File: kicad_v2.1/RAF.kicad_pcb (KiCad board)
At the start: 2 copper layers, 68.6 x 53.3 mm, 44 parts, among them J1 SERVO, J2 SERVO, J3 SOL, J4 SERVO, J5 PUMP, J6 WS2811-OUT, J7 I2C, P1 Power, P2 Analog, P3 Digital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

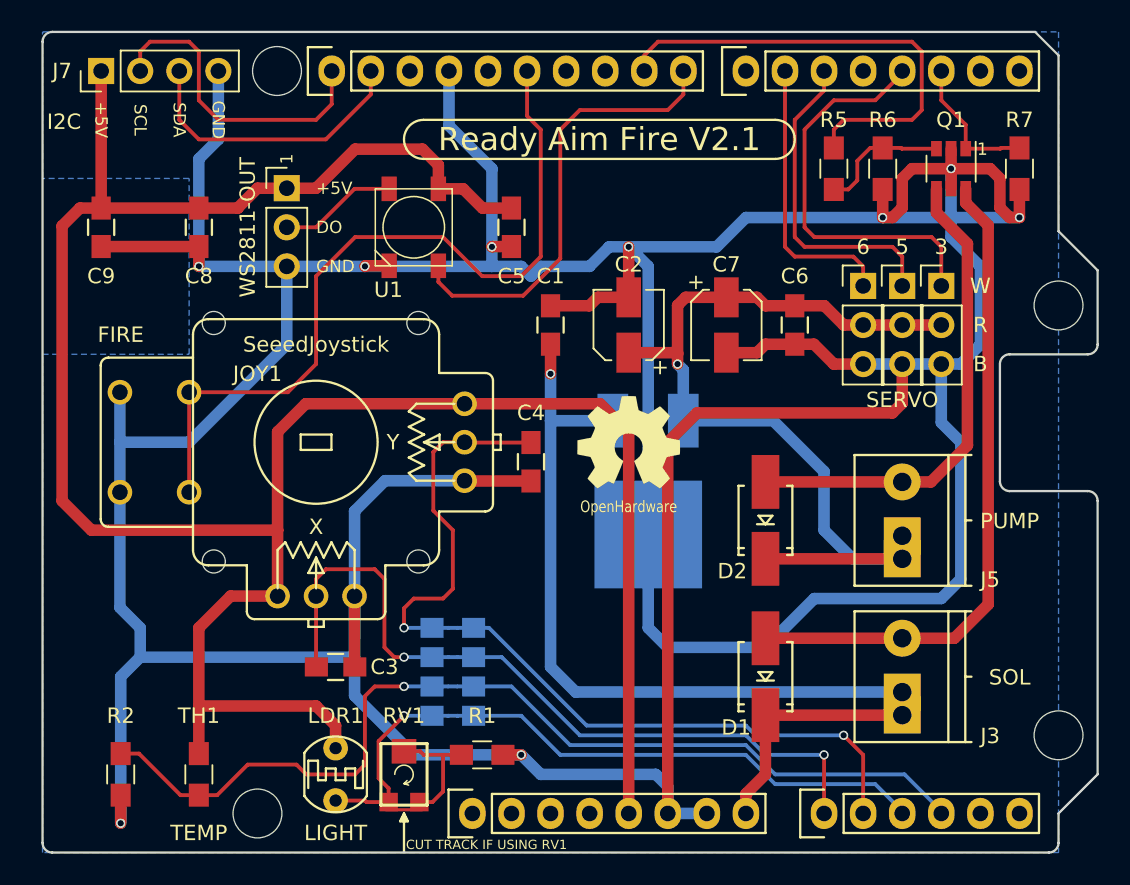
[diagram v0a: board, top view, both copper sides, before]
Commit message: joystick 3D updated
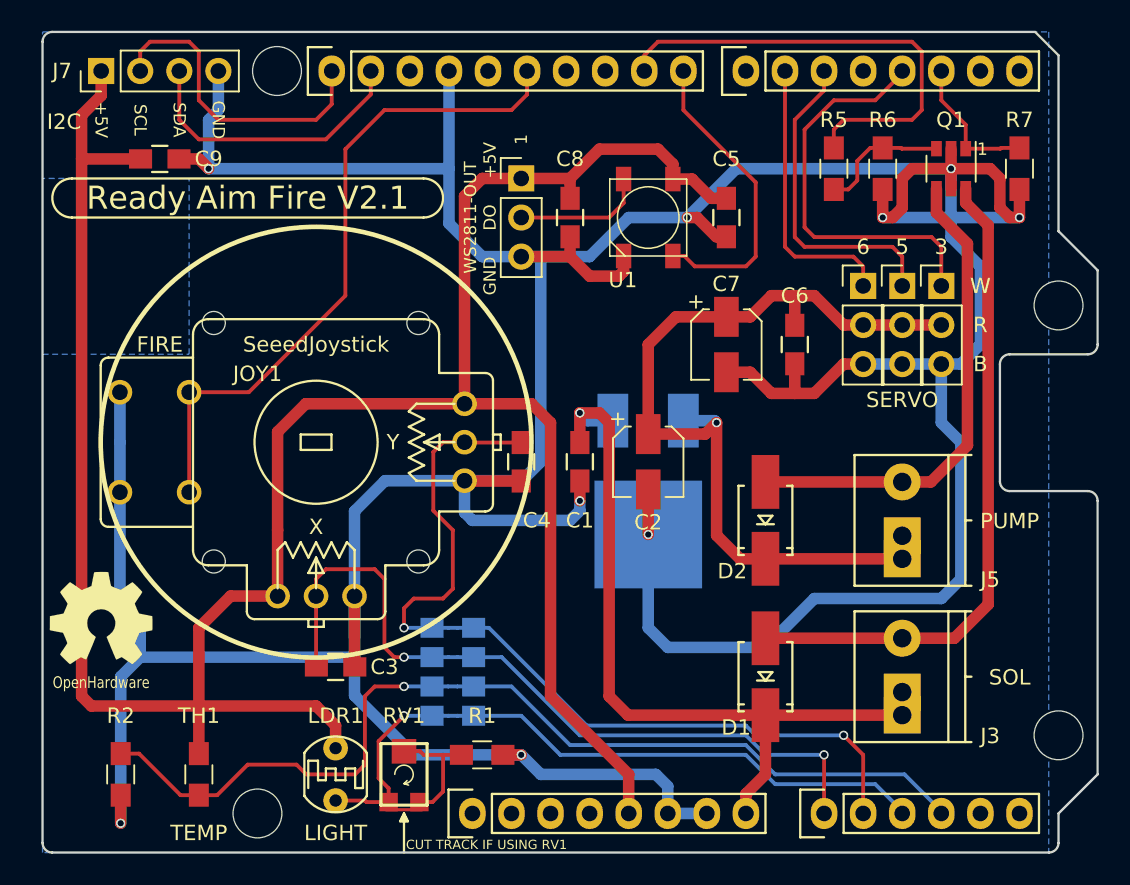
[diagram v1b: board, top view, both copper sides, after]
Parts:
- moved OSHW1 36.1 mm to (114.8, 111.1)
- moved C8 24.1 mm to (145.3, 85.1)
- moved U1 15.3 mm to (150.4, 85.1)
- moved J6 15.3 mm to (142.1, 82.5)
- moved C5 14.0 mm to (155.4, 85.1)
- moved C1 9.09 mm to (145.9, 101.0), turned to 270 degrees
- moved C2 8.98 mm to (150.4, 101.0), turned to 270 degrees
- moved C9 5.85 mm to (118.6, 81.3), turned to 0 degrees
- moved C6 1.27 mm to (159.9, 93.3)
- moved C7 1.27 mm to (155.4, 93.3)
- moved C4 0.63 mm to (142.1, 101.0)
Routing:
- net GND: track 379.9 -> 325.2 mm
- net /Vin: track 65.9 -> 52.2 mm
- net +5V: track 160.2 -> 170.1 mm
- net /8: track 29.2 -> 19.9 mm
- net /12(MISO): track 50.9 -> 43.6 mm
- net /SVCC: track 59.6 -> 57.4 mm
- net /LED_OUT: track 7.69 -> 8.60 mm
- net /A1: track 58.2 -> 57.6 mm

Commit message: added pogo connector for testing solenoid, pump, servo
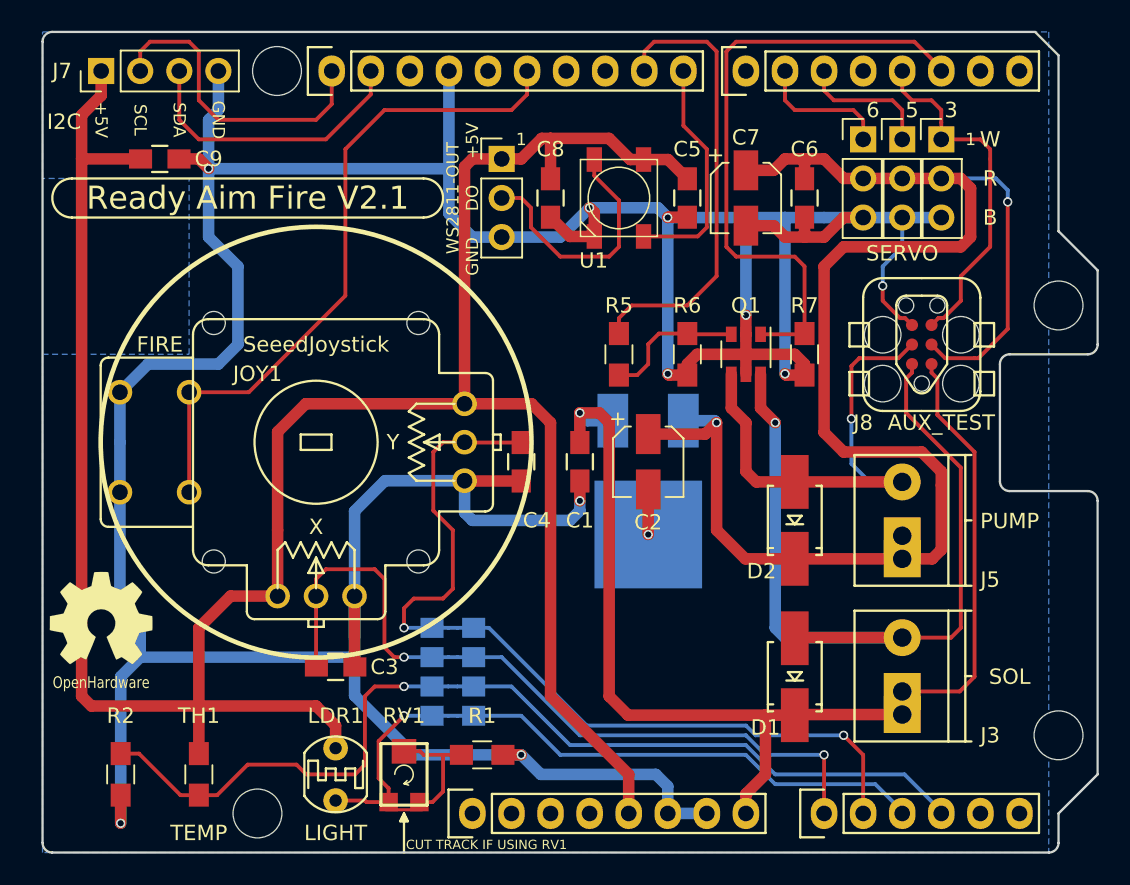
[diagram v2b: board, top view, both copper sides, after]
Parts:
- added J8: AUX_TEST, RAF_Libs:TC2030-IDC, F.Cu at (168.1, 95.9)
- moved R5 18.5 mm to (148.5, 94.0)
- moved R7 18.5 mm to (160.5, 94.0)
- moved Q1 18.0 mm to (156.7, 94.0)
- moved R6 17.5 mm to (152.9, 94.0)
- moved C7 9.61 mm to (156.7, 83.8)
- moved C6 9.55 mm to (160.5, 83.8)
- moved J1 9.52 mm to (169.4, 80.0)
- moved J2 9.52 mm to (166.9, 80.0)
- moved J4 9.52 mm to (164.3, 80.0)
- moved C5 2.84 mm to (152.9, 83.8)
- moved U1 2.29 mm to (148.5, 83.8)
- moved D1 1.91 mm to (159.9, 114.9)
- moved D2 1.91 mm to (159.9, 104.8)
- moved C8 1.80 mm to (144.0, 83.8)
- moved J6 1.80 mm to (140.8, 81.3)
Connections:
- net Net-(D1-Pad2) renamed /SOL
- net Net-(D2-Pad2) renamed /PUMP
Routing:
- net GND: track 325.2 -> 275.0 mm, vias 9 -> 11
- net /SVCC: track 57.4 -> 105.9 mm, vias 1 -> 2
- net /2: track 9.22 -> 40.7 mm
- net /Vin: track 52.2 -> 78.8 mm
- net /SOL: track 43.0 -> 55.2 mm, vias 0 -> 1
- net /5(**): track 21.0 -> 8.78 mm
- net /6(**): track 18.3 -> 8.78 mm
- net /LED_OUT: track 8.60 -> 16.5 mm
- net /8: track 19.9 -> 15.2 mm
- net /3(**): track 26.3 -> 23.0 mm
- net /9(**): track 30.9 -> 29.6 mm
- net Net-(Q1-Pad3): track 8.55 -> 9.20 mm
- net +5V: track 170.1 -> 169.5 mm
- net /PUMP: track 31.6 -> 31.8 mm, vias 0 -> 1

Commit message: cleaned up silk legend
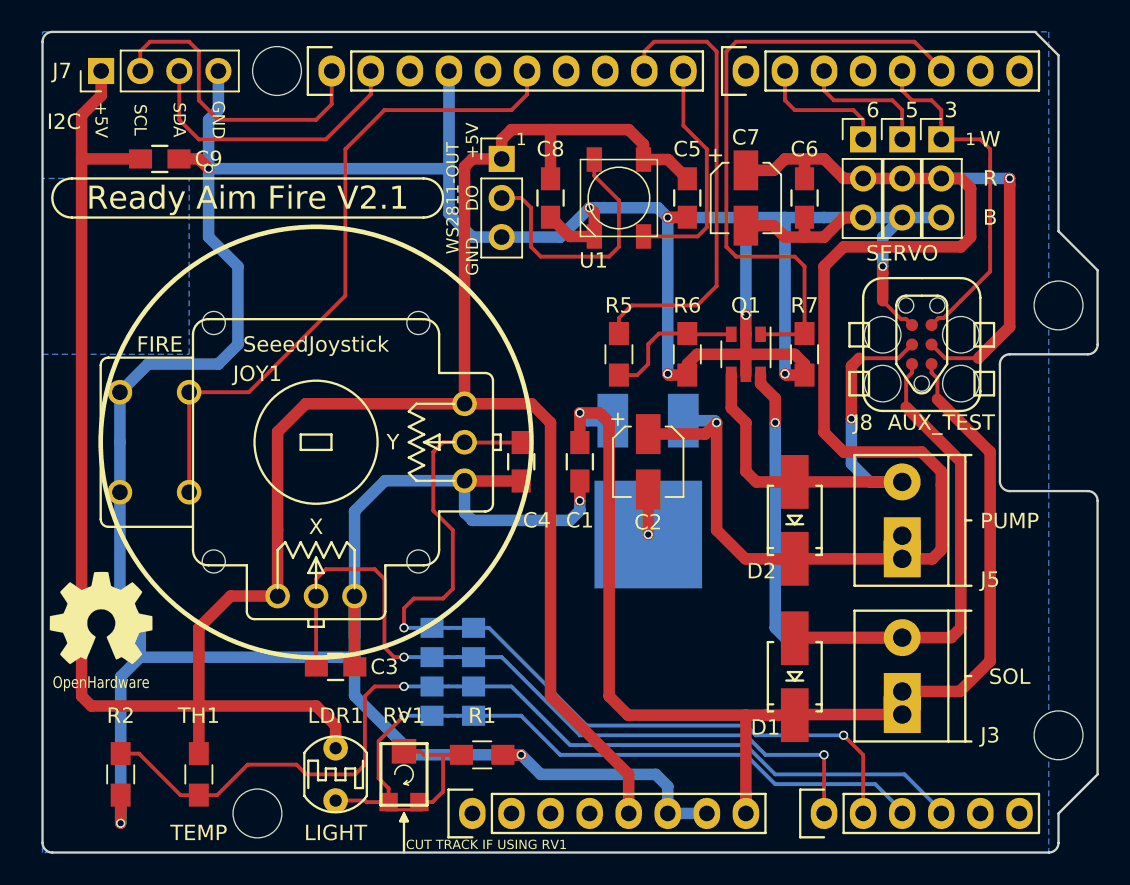
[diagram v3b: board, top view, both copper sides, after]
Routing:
- net +5V: track 169.5 -> 171.8 mm
- net /Vin: track 78.8 -> 80.4 mm
- net /LED_OUT: track 16.5 -> 17.3 mm
- net /SVCC: track 105.9 -> 106.5 mm
